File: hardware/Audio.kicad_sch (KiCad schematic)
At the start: 48 parts, among them IC301 LM4991xx, J301 CAT_TX, J302 CAT_RX, Q301 IRLML2060, Q302 BSS138, Q303 BSS138, U301 MCP6002, U302 MAX9814

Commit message: Replaced pkl footprints with kicad standard library footprints
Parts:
- C301, C302, C303, C304, C305, C306, C307, C308, C309, C310, C312, C313, C314, C315, C316, C318: footprint pkl_dipol:C_0603 -> Capacitor_SMD:C_0603_1608Metric
- J301, J302: footprint pkl_jumpers:J_NCNO_0903_20 -> Jumper:SolderJumper-3_P1.3mm_Bridged12_RoundedPad1.0x1.5mm
- Q301: footprint pkl_housings_sot:SOT-23 -> Package_TO_SOT_SMD:SOT-23
- R301, R302, R303, R304, R305, R306, R307, R308, R309, R310, R311, R312, R313, R314, R315, R316, R317, R318: footprint pkl_dipol:R_0603 -> Resistor_SMD:R_0603_1608Metric
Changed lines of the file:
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@@
       (effects (font (size 1.27 1.27)) (justify left))
     )
-    (property "Footprint" "pkl_dipol:C_0603" (at 153.67 115.57 0)
+    (property "Footprint" "Capacitor_SMD:C_0603_1608Metric" (at 153.67 115.57 0)
       (effects (font (size 1.524 1.524)) hide)
     )
@@
       (effects (font (size 1.27 1.27)) (justify left))
     )
-    (property "Footprint" "pkl_dipol:C_0603" (at 163.83 115.57 0)
+    (property "Footprint" "Capacitor_SMD:C_0603_1608Metric" (at 163.83 115.57 0)
       (effects (font (size 1.524 1.524)) hide)
     )
@@
       (effects (font (size 1.27 1.27)) (justify left))
     )
-    (property "Footprint" "pkl_dipol:C_0603" (at 191.77 40.64 0)
+    (property "Footprint" "Capacitor_SMD:C_0603_1608Metric" (at 191.77 40.64 0)
       (effects (font (size 1.524 1.524)) hide)
     )
@@
       (effects (font (size 1.27 1.27)) (justify left))
     )
-    (property "Footprint" "pkl_dipol:R_0603" (at 27.94 182.88 0)
+    (property "Footprint" "Resistor_SMD:R_0603_1608Metric" (at 27.94 182.88 0)
       (effects (font (size 1.524 1.524)) hide)
     )
@@
       (effects (font (size 1.27 1.27)))
     )
-    (property "Footprint" "pkl_dipol:R_0603" (at 33.02 177.8 0)
+    (property "Footprint" "Resistor_SMD:R_0603_1608Metric" (at 33.02 177.8 0)
       (effects (font (size 1.524 1.524)) hide)
     )
@@
       (effects (font (size 1.27 1.27)) (justify left))
     )
-    (property "Footprint" "pkl_dipol:C_0603" (at 38.1 182.88 0)
+    (property "Footprint" "Capacitor_SMD:C_0603_1608Metric" (at 38.1 182.88 0)
       (effects (font (size 1.524 1.524)) hide)
     )
@@
       (effects (font (size 1.27 1.27)) (justify left))
     )
-    (property "Footprint" "pkl_housings_sot:SOT-23" (at 50.8 179.705 0)
+    (property "Footprint" "Package_TO_SOT_SMD:SOT-23" (at 50.8 179.705 0)
       (effects (font (size 1.27 1.27) italic) (justify left) hide)
     )
@@
       (effects (font (size 1.27 1.27)))
     )
-    (property "Footprint" "pkl_dipol:C_0603" (at 50.8 129.54 0)
+    (property "Footprint" "Capacitor_SMD:C_0603_1608Metric" (at 50.8 129.54 0)
       (effects (font (size 1.524 1.524)) hide)
     )
@@
       (effects (font (size 1.27 1.27)) (justify left))
     )
-    (property "Footprint" "pkl_dipol:R_0603" (at 50.8 137.16 0)
+    (property "Footprint" "Resistor_SMD:R_0603_1608Metric" (at 50.8 137.16 0)
       (effects (font (size 1.524 1.524)) hide)
     )
@@
       (effects (font (size 1.27 1.27)))
     )
-    (property "Footprint" "pkl_dipol:R_0603" (at 125.73 54.61 0)
+    (property "Footprint" "Resistor_SMD:R_0603_1608Metric" (at 125.73 54.61 0)
       (effects (font (size 1.524 1.524)) hide)
     )
@@
       (effects (font (size 1.27 1.27)) (justify left))
     )
-    (property "Footprint" "pkl_jumpers:J_NCNO_0903_20" (at 106.045 181.61 0)
+    (property "Footprint" "Jumper:SolderJumper-3_P1.3mm_Bridged12_RoundedPad1.0x1.5mm" (at 106.045 181.61 0)
       (effects (font (size 1.27 1.27)) hide)
     )
@@
       (effects (font (size 1.27 1.27)) (justify left))
     )
-    (property "Footprint" "pkl_jumpers:J_NCNO_0903_20" (at 133.985 181.61 0)
+    (property "Footprint" "Jumper:SolderJumper-3_P1.3mm_Bridged12_RoundedPad1.0x1.5mm" (at 133.985 181.61 0)
       (effects (font (size 1.27 1.27)) hide)
     )
@@
       (effects (font (size 1.27 1.27)) (justify left))
     )
-    (property "Footprint" "pkl_dipol:R_0603" (at 161.29 182.88 0)
+    (property "Footprint" "Resistor_SMD:R_0603_1608Metric" (at 161.29 182.88 0)
       (effects (font (size 1.524 1.524)) hide)
     )
@@
       (effects (font (size 1.27 1.27)) (justify left))
     )
-    (property "Footprint" "pkl_dipol:C_0603" (at 38.735 77.47 0)
+    (property "Footprint" "Capacitor_SMD:C_0603_1608Metric" (at 38.735 77.47 0)
       (effects (font (size 1.524 1.524)) hide)
     )
@@
       (effects (font (size 1.27 1.27)))
     )
-    (property "Footprint" "pkl_dipol:C_0603" (at 73.66 36.195 0)
+    (property "Footprint" "Capacitor_SMD:C_0603_1608Metric" (at 73.66 36.195 0)
       (effects (font (size 1.27 1.27)) hide)
     )
@@
       (effects (font (size 1.27 1.27)) (justify left))
     )
-    (property "Footprint" "pkl_dipol:C_0603" (at 176.53 59.69 0)
+    (property "Footprint" "Capacitor_SMD:C_0603_1608Metric" (at 176.53 59.69 0)
       (effects (font (size 1.524 1.524)) hide)
     )
@@
       (effects (font (size 1.27 1.27)) (justify left))
     )
-    (property "Footprint" "pkl_dipol:R_0603" (at 146.05 182.88 0)
+    (property "Footprint" "Resistor_SMD:R_0603_1608Metric" (at 146.05 182.88 0)
       (effects (font (size 1.524 1.524)) hide)
     )
@@
       (effects (font (size 1.27 1.27)) (justify left))
     )
-    (property "Footprint" "pkl_dipol:C_0603" (at 53.34 53.975 0)
+    (property "Footprint" "Capacitor_SMD:C_0603_1608Metric" (at 53.34 53.975 0)
       (effects (font (size 1.27 1.27)) hide)
     )
@@
       (effects (font (size 1.27 1.27)))
     )
-    (property "Footprint" "pkl_dipol:R_0603" (at 64.77 46.99 0)
+    (property "Footprint" "Resistor_SMD:R_0603_1608Metric" (at 64.77 46.99 0)
       (effects (font (size 1.27 1.27)) hide)
     )
@@
       (effects (font (size 1.27 1.27)))
     )
-    (property "Footprint" "pkl_dipol:R_0603" (at 152.4 36.83 0)
+    (property "Footprint" "Resistor_SMD:R_0603_1608Metric" (at 152.4 36.83 0)
       (effects (font (size 1.524 1.524)) hide)
     )
@@
       (effects (font (size 1.27 1.27)))
     )
-    (property "Footprint" "pkl_dipol:R_0603" (at 48.895 46.99 0)
+    (property "Footprint" "Resistor_SMD:R_0603_1608Metric" (at 48.895 46.99 0)
       (effects (font (size 1.27 1.27)) hide)
     )
@@
       (effects (font (size 1.27 1.27)) (justify left))
     )
-    (property "Footprint" "pkl_dipol:R_0603" (at 73.025 182.88 0)
+    (property "Footprint" "Resistor_SMD:R_0603_1608Metric" (at 73.025 182.88 0)
       (effects (font (size 1.524 1.524)) hide)
     )
@@
       (effects (font (size 1.27 1.27)) (justify right))
     )
-    (property "Footprint" "pkl_dipol:R_0603" (at 69.85 74.93 0)
+    (property "Footprint" "Resistor_SMD:R_0603_1608Metric" (at 69.85 74.93 0)
       (effects (font (size 1.27 1.27)) hide)
     )
@@
       (effects (font (size 1.27 1.27)) (justify left))
     )
-    (property "Footprint" "pkl_dipol:C_0603" (at 76.2 142.24 0)
+    (property "Footprint" "Capacitor_SMD:C_0603_1608Metric" (at 76.2 142.24 0)
       (effects (font (size 1.524 1.524)) hide)
     )
@@
       (effects (font (size 1.27 1.27)) (justify left))
     )
-    (property "Footprint" "pkl_dipol:C_0603" (at 55.88 142.24 0)
+    (property "Footprint" "Capacitor_SMD:C_0603_1608Metric" (at 55.88 142.24 0)
       (effects (font (size 1.524 1.524)) hide)
     )
@@
       (effects (font (size 1.27 1.27)) (justify left))
     )
-    (property "Footprint" "pkl_dipol:R_0603" (at 176.53 67.31 0)
+    (property "Footprint" "Resistor_SMD:R_0603_1608Metric" (at 176.53 67.31 0)
       (effects (font (size 1.524 1.524)) hide)
     )
@@
       (effects (font (size 1.27 1.27)))
     )
-    (property "Footprint" "pkl_dipol:C_0603" (at 152.4 27.94 0)
+    (property "Footprint" "Capacitor_SMD:C_0603_1608Metric" (at 152.4 27.94 0)
       (effects (font (size 1.524 1.524)) hide)
     )
@@
       (effects (font (size 1.27 1.27)) (justify left))
     )
-    (property "Footprint" "pkl_dipol:C_0603" (at 133.35 59.69 0)
+    (property "Footprint" "Capacitor_SMD:C_0603_1608Metric" (at 133.35 59.69 0)
       (effects (font (size 1.524 1.524)) hide)
     )
@@
       (effects (font (size 1.27 1.27)))
     )
-    (property "Footprint" "pkl_dipol:C_0603" (at 118.11 54.61 0)
+    (property "Footprint" "Capacitor_SMD:C_0603_1608Metric" (at 118.11 54.61 0)
       (effects (font (size 1.524 1.524)) hide)
     )
@@
       (effects (font (size 1.27 1.27)))
     )
-    (property "Footprint" "pkl_dipol:R_0603" (at 57.15 46.99 0)
+    (property "Footprint" "Resistor_SMD:R_0603_1608Metric" (at 57.15 46.99 0)
       (effects (font (size 1.27 1.27)) hide)
     )
@@
       (effects (font (size 1.27 1.27)))
     )
-    (property "Footprint" "pkl_dipol:R_0603" (at 71.12 127 0)
+    (property "Footprint" "Resistor_SMD:R_0603_1608Metric" (at 71.12 127 0)
       (effects (font (size 1.524 1.524)) hide)
     )
@@
       (effects (font (size 1.27 1.27)) (justify left))
     )
-    (property "Footprint" "pkl_dipol:R_0603" (at 66.04 142.24 0)
+    (property "Footprint" "Resistor_SMD:R_0603_1608Metric" (at 66.04 142.24 0)
       (effects (font (size 1.524 1.524)) hide)
     )
@@
       (effects (font (size 1.27 1.27)) (justify left))
     )
-    (property "Footprint" "pkl_dipol:R_0603" (at 88.265 182.88 0)
+    (property "Footprint" "Resistor_SMD:R_0603_1608Metric" (at 88.265 182.88 0)
       (effects (font (size 1.524 1.524)) hide)
     )
@@
       (effects (font (size 1.27 1.27)) (justify left))
     )
-    (property "Footprint" "pkl_dipol:C_0603" (at 85.09 142.24 0)
+    (property "Footprint" "Capacitor_SMD:C_0603_1608Metric" (at 85.09 142.24 0)
       (effects (font (size 1.524 1.524)) hide)
     )
@@
       (effects (font (size 1.27 1.27)) (justify right))
     )
-    (property "Footprint" "pkl_dipol:R_0603" (at 69.85 81.915 0)
+    (property "Footprint" "Resistor_SMD:R_0603_1608Metric" (at 69.85 81.915 0)
       (effects (font (size 1.27 1.27)) hide)
     )
@@
       (effects (font (size 1.27 1.27)) (justify left))
     )
-    (property "Footprint" "pkl_dipol:C_0603" (at 68.58 53.975 0)
+    (property "Footprint" "Capacitor_SMD:C_0603_1608Metric" (at 68.58 53.975 0)
       (effects (font (size 1.27 1.27)) hide)
     )
@@
       (effects (font (size 1.27 1.27)) (justify left))
     )
-    (property "Footprint" "pkl_dipol:R_0603" (at 41.91 124.46 0)
-      (effects (font (size 1.524 1.524)) hide)
-    )
+    (property "Footprint" "Resistor_SMD:R_0603_1608Metric" (at 41.91 124.46 0)
+      (effects (font (size 1.524 1.524)) hide)
+    )

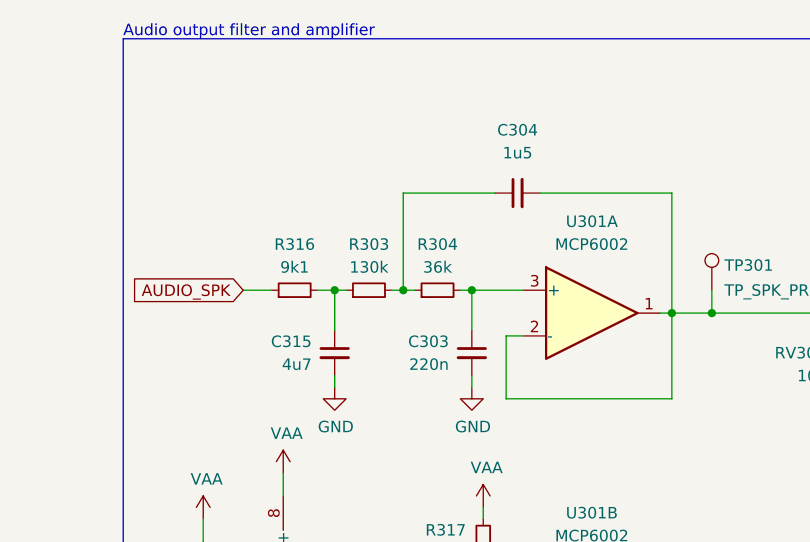
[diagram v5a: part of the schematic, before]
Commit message: Updated logos in schematic
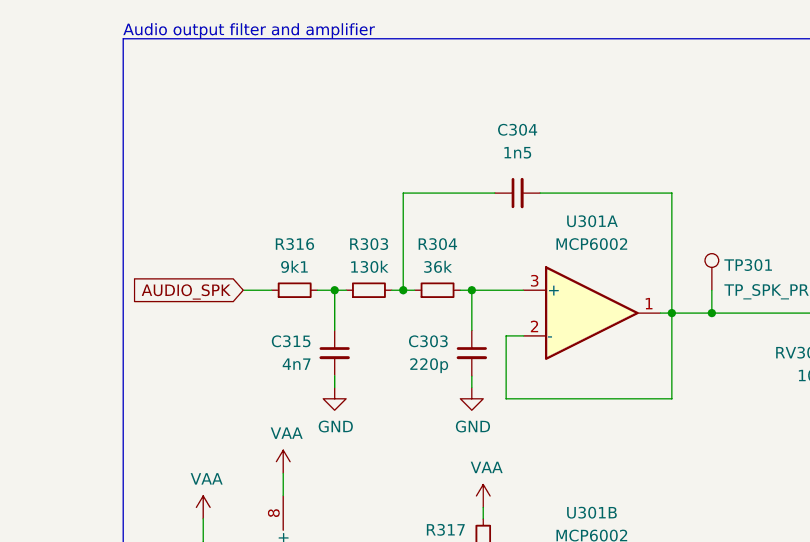
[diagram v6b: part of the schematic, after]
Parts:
- C303: value 220n -> 220p; MPN Generic C 220n/X7R/10V/0603 -> Generic C 220p/X7R/10V/0603
- C304: value 1u5 -> 1n5; MPN Generic C 1u5/X7R/10V/0603 -> Generic C 1n5/X7R/10V/0603
- C315: value 4u7 -> 4n7; MPN Generic C 4u7/X7R/10V/0603 -> Generic C 4n7/X7R/10V/0603
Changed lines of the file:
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@@
       (effects (font (size 1.27 1.27)))
     )
-    (property "Value" "1u5" (at 73.6663 31.75 90)
+    (property "Value" "1n5" (at 73.6663 31.75 90)
       (effects (font (size 1.27 1.27)))
     )
@@
       (effects (font (size 1.27 1.27)) hide)
     )
-    (property "MPN" "Generic C 1u5/X7R/10V/0603" (at 73.66 36.195 0)
+    (property "MPN" "Generic C 1n5/X7R/10V/0603" (at 73.66 36.195 0)
       (effects (font (size 1.27 1.27)) hide)
     )
@@
       (effects (font (size 1.27 1.27)) (justify left))
     )
-    (property "Value" "4u7" (at 50.8 55.2513 0)
+    (property "Value" "4n7" (at 50.8 55.2513 0)
       (effects (font (size 1.27 1.27)) (justify left))
     )
@@
       (effects (font (size 1.27 1.27)) hide)
     )
-    (property "MPN" "Generic C 4u7/X7R/10V/0603" (at 53.34 53.975 0)
+    (property "MPN" "Generic C 4n7/X7R/10V/0603" (at 53.34 53.975 0)
       (effects (font (size 1.27 1.27)) hide)
     )
@@
       (effects (font (size 1.27 1.27)) (justify left))
     )
-    (property "Value" "220n" (at 66.04 55.2513 0)
+    (property "Value" "220p" (at 66.04 55.2513 0)
       (effects (font (size 1.27 1.27)) (justify left))
     )
@@
       (effects (font (size 1.27 1.27)) hide)
     )
-    (property "MPN" "Generic C 220n/X7R/10V/0603" (at 68.58 53.975 0)
-      (effects (font (size 1.27 1.27)) hide)
-    )
+    (property "MPN" "Generic C 220p/X7R/10V/0603" (at 68.58 53.975 0)
+      (effects (font (size 1.27 1.27)) hide)
+    )

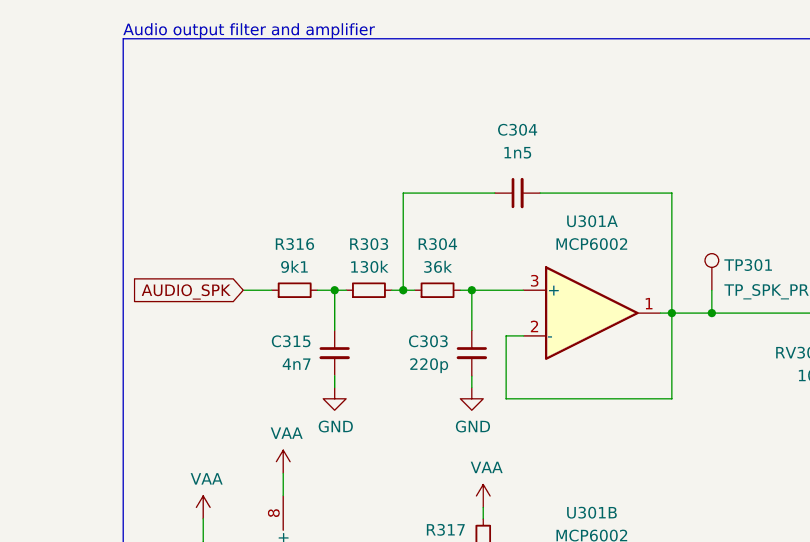
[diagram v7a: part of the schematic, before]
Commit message: Updated audio output filter, updated OHIS connector
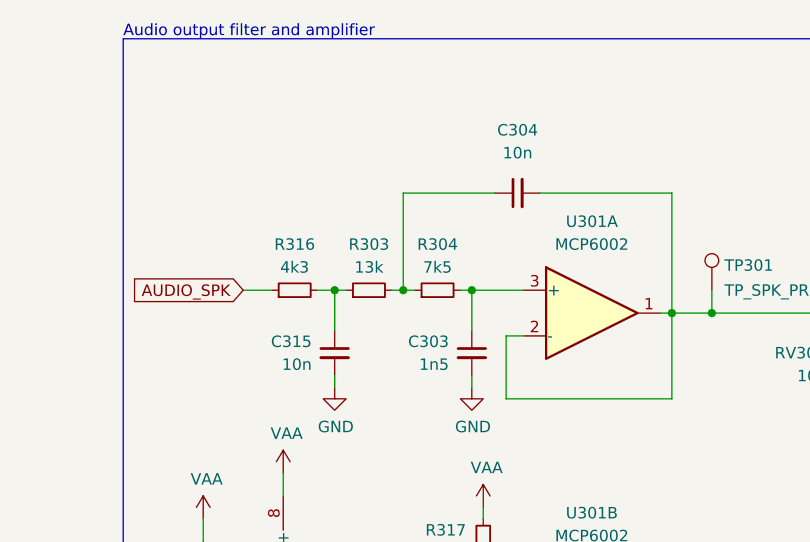
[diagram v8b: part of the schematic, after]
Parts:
- C303: value 220p -> 1n5; MPN Generic C 220p/X7R/10V/0603 -> Generic C 1n5/X7R/10V/0603
- C304: value 1n5 -> 10n; MPN Generic C 1n5/X7R/10V/0603 -> Generic C 10n/X7R/10V/0603
- C315: value 4n7 -> 10n; MPN Generic C 4n7/X7R/10V/0603 -> Generic C 10n/X7R/10V/0603
- R303: value 130k -> 13k; MPN Generic R/130k/0603 -> Generic R/13k/0603
- R304: value 36k -> 7k5; MPN Generic R/36k/0603 -> Generic R/7k5/0603
- R316: value 9k1 -> 4k3; MPN Generic R/9k1/0603 -> Generic R/4k3/0603
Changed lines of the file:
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@@
       (effects (font (size 1.27 1.27)))
     )
-    (property "Value" "1n5" (at 73.6663 31.75 90)
+    (property "Value" "10n" (at 73.6663 31.75 90)
       (effects (font (size 1.27 1.27)))
     )
@@
       (effects (font (size 1.27 1.27)) hide)
     )
-    (property "MPN" "Generic C 1n5/X7R/10V/0603" (at 73.66 36.195 0)
+    (property "MPN" "Generic C 10n/X7R/10V/0603" (at 73.66 36.195 0)
       (effects (font (size 1.27 1.27)) hide)
     )
@@
       (effects (font (size 1.27 1.27)) (justify left))
     )
-    (property "Value" "4n7" (at 50.8 55.2513 0)
+    (property "Value" "10n" (at 50.8 55.2513 0)
       (effects (font (size 1.27 1.27)) (justify left))
     )
@@
       (effects (font (size 1.27 1.27)) hide)
     )
-    (property "MPN" "Generic C 4n7/X7R/10V/0603" (at 53.34 53.975 0)
+    (property "MPN" "Generic C 10n/X7R/10V/0603" (at 53.34 53.975 0)
       (effects (font (size 1.27 1.27)) hide)
     )
@@
       (effects (font (size 1.27 1.27)))
     )
-    (property "Value" "36k" (at 64.77 44.45 90)
+    (property "Value" "7k5" (at 64.77 44.45 90)
       (effects (font (size 1.27 1.27)))
     )
@@
       (effects (font (size 1.27 1.27)) hide)
     )
-    (property "MPN" "Generic R/36k/0603" (at 64.77 46.99 90)
+    (property "MPN" "Generic R/7k5/0603" (at 64.77 46.99 90)
       (effects (font (size 1.27 1.27)) hide)
     )
@@
       (effects (font (size 1.27 1.27)))
     )
-    (property "Value" "9k1" (at 48.895 44.45 90)
+    (property "Value" "4k3" (at 48.895 44.45 90)
       (effects (font (size 1.27 1.27)))
     )
@@
       (effects (font (size 1.27 1.27)) hide)
     )
-    (property "MPN" "Generic R/9k1/0603" (at 48.895 46.99 90)
+    (property "MPN" "Generic R/4k3/0603" (at 48.895 46.99 90)
       (effects (font (size 1.27 1.27)) hide)
     )
@@
       (effects (font (size 1.27 1.27)))
     )
-    (property "Value" "130k" (at 57.15 44.45 90)
+    (property "Value" "13k" (at 57.15 44.45 90)
       (effects (font (size 1.27 1.27)))
     )
@@
       (effects (font (size 1.27 1.27)) hide)
     )
-    (property "MPN" "Generic R/130k/0603" (at 57.15 46.99 90)
+    (property "MPN" "Generic R/13k/0603" (at 57.15 46.99 90)
       (effects (font (size 1.27 1.27)) hide)
     )
@@
       (effects (font (size 1.27 1.27)) (justify left))
     )
-    (property "Value" "220p" (at 66.04 55.2513 0)
+    (property "Value" "1n5" (at 66.04 55.2513 0)
       (effects (font (size 1.27 1.27)) (justify left))
     )
@@
       (effects (font (size 1.27 1.27)) hide)
     )
-    (property "MPN" "Generic C 220p/X7R/10V/0603" (at 68.58 53.975 0)
-      (effects (font (size 1.27 1.27)) hide)
-    )
+    (property "MPN" "Generic C 1n5/X7R/10V/0603" (at 68.58 53.975 0)
+      (effects (font (size 1.27 1.27)) hide)
+    )
